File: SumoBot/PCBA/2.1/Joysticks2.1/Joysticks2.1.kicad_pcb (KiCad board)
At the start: 2 copper layers, 113.5 x 60.8 mm, 22 parts, among them J1 Screw_Terminal_01x02, J4 OLED SCREEN, U1 THB001P, U11 THB001P, U2 MX1A-11NN, U3 MX1A-11NN, U4 MX1A-11NN, U5 MX1A-11NN, U6 NRF24L01_Breakout

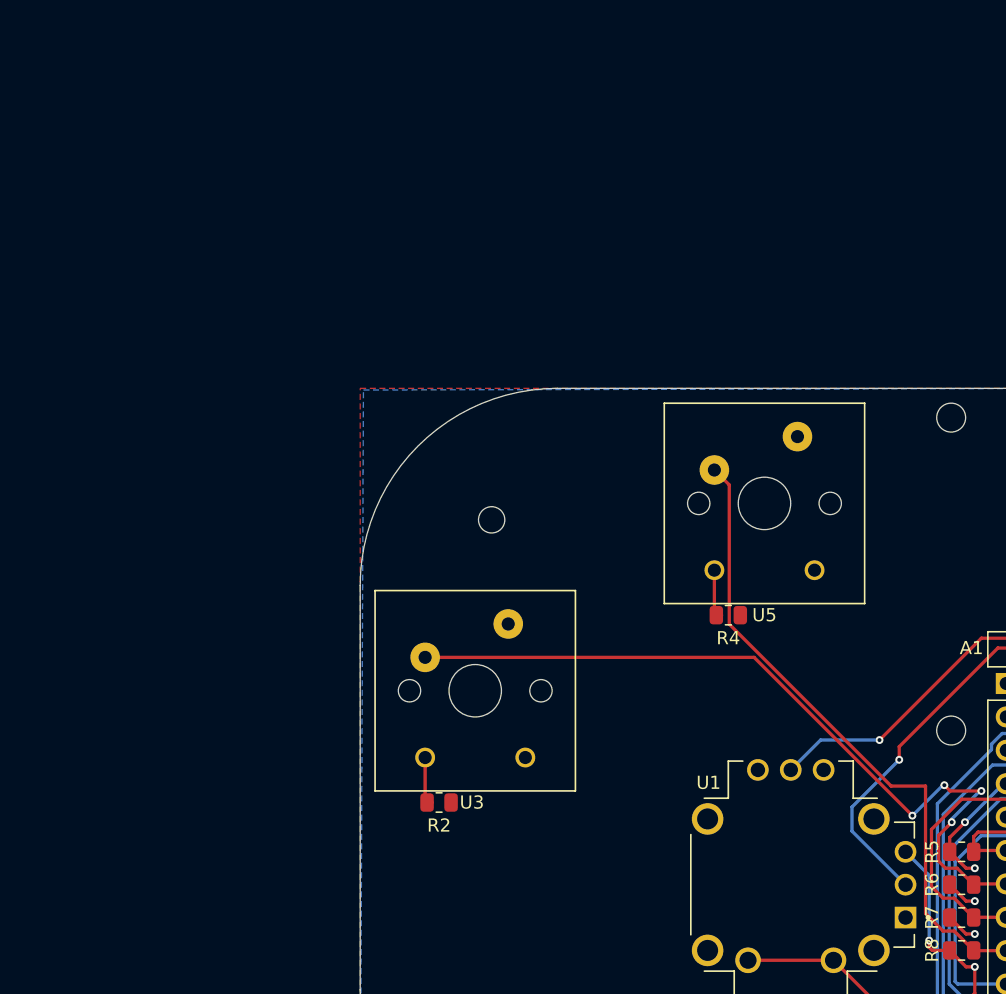
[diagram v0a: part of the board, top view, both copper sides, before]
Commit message: added notes to sumonyx pcbs
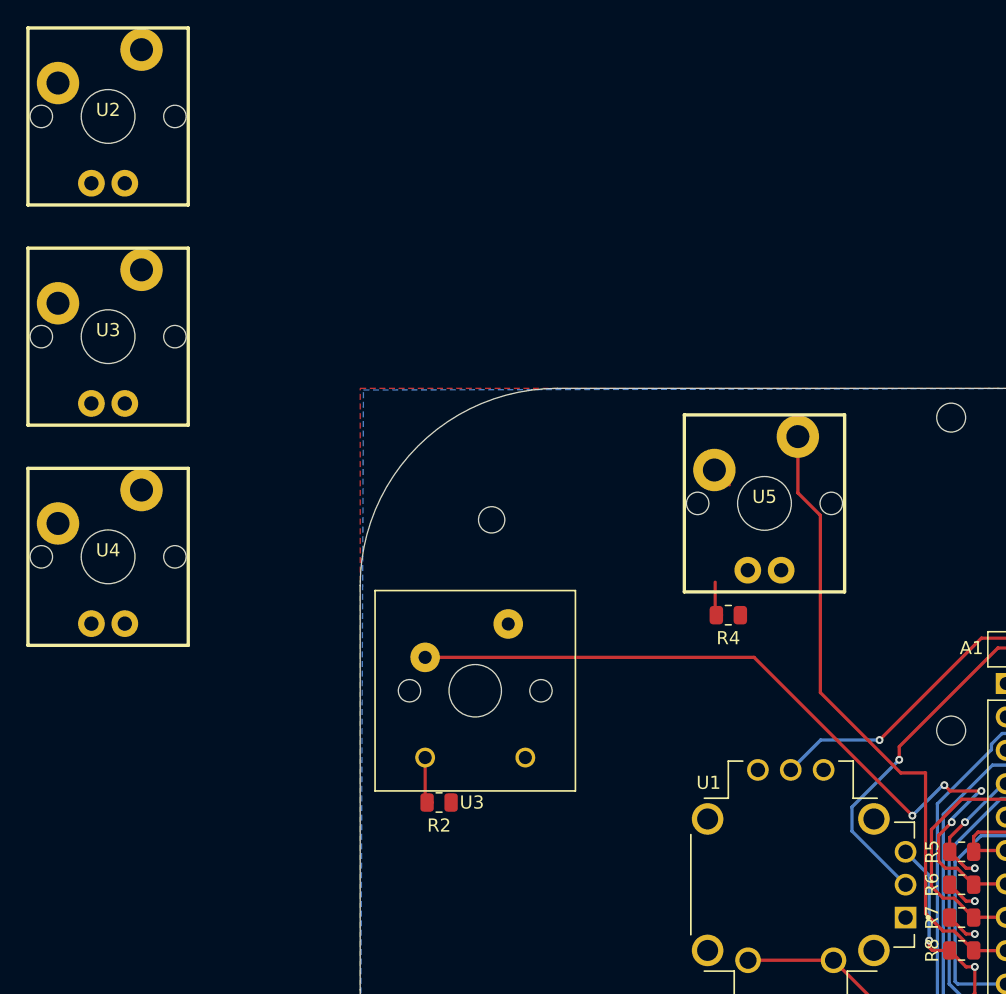
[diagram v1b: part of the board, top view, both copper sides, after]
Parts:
- added U2: ~, Button_Switch_Keyboard:SW_Cherry_MX_3mmLED, F.Cu at (24.1, 50.6)
- added U3: ~, Button_Switch_Keyboard:SW_Cherry_MX_3mmLED, F.Cu at (24.1, 67.3)
- added U4: ~, Button_Switch_Keyboard:SW_Cherry_MX_3mmLED, F.Cu at (24.1, 84.1)
- U5: value MX1A-11NN -> ~; footprint MX1A-11NN:CHERRY_MX1A-11NN_SWITCH -> Button_Switch_Keyboard:SW_Cherry_MX_3mmLED
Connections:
- A1 pad 6: Net-(A1-Pad6) -> Net-(A1-D3)
- A1 pad 9: Net-(A1-Pad9) -> Net-(A1-D6)
- R4 pad 1: Net-(R4-Pad1) -> Net-(U5-A)
- R5 pad 2: Net-(A1-Pad6) -> Net-(A1-D3)
- R8 pad 2: Net-(A1-Pad9) -> Net-(A1-D6)
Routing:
- net Net-(A1-Pad9): track 49.2 -> 0.00 mm
- net Net-(A1-D6): track 0.00 -> 48.7 mm
- net Net-(R4-Pad1): track 3.65 -> 0.00 mm
- net Net-(U5-A): track 0.00 -> 2.70 mm
- net +6V: track 0.00 -> 1.61 mm
